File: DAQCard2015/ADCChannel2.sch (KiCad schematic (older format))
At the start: 16 parts, among them U17 THS4524IDBTR, U18 AD9219

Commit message: Various updates to DAQ board focusing on power system
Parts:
- U17: footprint Housings_SSOP:TSSOP-38_4.4x9.7mm_Pitch0.5mm -> extras:TSSOP-38_4.4x9.7mm_Pitch0.5mm
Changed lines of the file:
@@
 F 0 "U17" H 4700 2750 60  0000 C CNN
 F 1 "THS4524IDBTR" H 4400 4850 60  0000 C CNN
-F 2 "Housings_SSOP:TSSOP-38_4.4x9.7mm_Pitch0.5mm" H 4600 3800 60  0001 C CNN
+F 2 "extras:TSSOP-38_4.4x9.7mm_Pitch0.5mm" H 4600 3800 60  0001 C CNN
 F 3 "" H 4600 3800 60  0000 C CNN
 	1    4400 3700

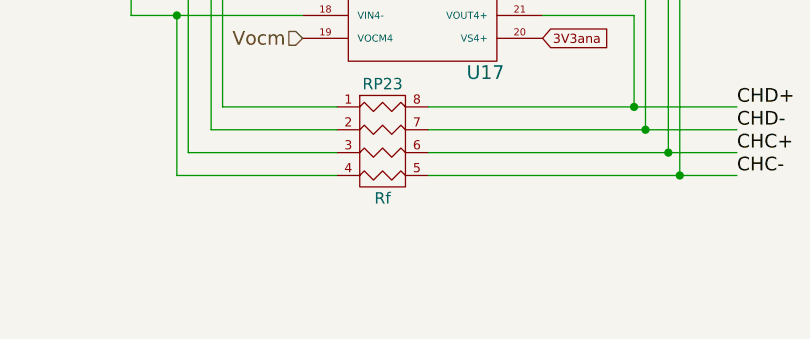
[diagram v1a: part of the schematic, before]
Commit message: Update to DAQ Board including adding an JTAG header and hooking up external clock and trigger
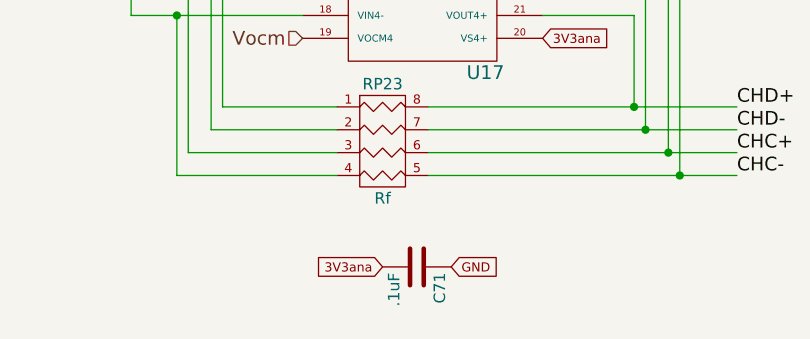
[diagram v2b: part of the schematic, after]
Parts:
- added C71: .1uF, Capacitors_SMD:C_0603, symbol C
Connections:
- net 3V3ana: now also C71.2
- net GND: now also C71.1
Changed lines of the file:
@@
 $Descr A4 11693 8268
 encoding utf-8
-Sheet 9 13
+Sheet 12 13
 Title ""
 Date ""
@@
 Text GLabel 8100 4150 0    40   Input ~ 0
 GND
+$Comp
+L C C71
+U 1 1 56064449
+P 4400 5500
+F 0 "C71" H 4425 5600 50  0000 L CNN
+F 1 ".1uF" H 4425 5400 50  0000 L CNN
+F 2 "Capacitors_SMD:C_0603" H 4438 5350 30  0001 C CNN
+F 3 "" H 4400 5500 60  0000 C CNN
+	1    4400 5500
+	0    1    1    0
+$EndComp
+Text GLabel 4250 5500 0    40   Input ~ 0
+3V3ana
+Text GLabel 4550 5500 2    40   Input ~ 0
+GND
 $EndSCHEMATC

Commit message: Adds digipart field to all parts that is now used in automatic generation of BOM(see DAQCard2015.html)
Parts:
- C47, C48, C49, C51, C52, C71: digipart (none) -> 445-1316-1-ND
- C50: digipart (none) -> 445-1420-1-ND
- R41, R42, R43, R44: digipart (none) -> P107HCT-ND
- R45: digipart (none) -> P10.0KHCT-ND
- RP22: digipart (none) -> RHM1564CT-ND
- RP23, RP24: digipart (none) -> RHM1336CT-ND
- U17: digipart (none) -> 296-24315-1-ND
- U18: digipart (none) -> AD9219ABCPZ-40-ND
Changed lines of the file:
@@
 F 2 "extras:QFN-48-1EP" H 8650 3700 60  0001 C CNN
 F 3 "" H 8650 3700 60  0000 C CNN
+F 4 "AD9219ABCPZ-40-ND" H 9050 3700 60  0001 C CNN "digipart"
 	1    9050 3700
 	1    0    0    -1
@@
 F 2 "Capacitors_SMD:C_0603" H 7588 3500 30  0001 C CNN
 F 3 "" H 7550 3650 60  0000 C CNN
+F 4 "445-1316-1-ND" H 7550 3650 60  0001 C CNN "digipart"
 	1    7550 3650
 	0    1    1    0
@@
 F 2 "Capacitors_SMD:C_0603" H 7588 3800 30  0001 C CNN
 F 3 "" H 7550 3950 60  0000 C CNN
+F 4 "445-1316-1-ND" H 7550 3950 60  0001 C CNN "digipart"
 	1    7550 3950
 	0    1    1    0
@@
 F 2 "Capacitors_SMD:C_0603" H 9338 1600 30  0001 C CNN
 F 3 "" H 9300 1750 60  0000 C CNN
+F 4 "445-1316-1-ND" H 9300 1750 60  0001 C CNN "digipart"
 	1    9300 1750
 	0    1    1    0
@@
 F 2 "Capacitors_SMD:C_0603" H 8638 1600 30  0001 C CNN
 F 3 "" H 8600 1750 60  0000 C CNN
+F 4 "445-1316-1-ND" H 8600 1750 60  0001 C CNN "digipart"
 	1    8600 1750
 	0    1    1    0
@@
 F 2 "Capacitors_SMD:C_0603" H 8988 1500 30  0001 C CNN
 F 3 "" H 8950 1650 60  0000 C CNN
+F 4 "445-1316-1-ND" H 8950 1650 60  0001 C CNN "digipart"
 	1    8950 1650
 	0    1    1    0
@@
 F 2 "Resistors_SMD:R_0603" V 9830 1950 30  0001 C CNN
 F 3 "" H 9900 1950 30  0000 C CNN
+F 4 "P10.0KHCT-ND" V 9900 1950 60  0001 C CNN "digipart"
 	1    9900 1950
 	0    1    1    0
@@
 F 2 "extras:TSSOP-38_4.4x9.7mm_Pitch0.5mm" H 4600 3800 60  0001 C CNN
 F 3 "" H 4600 3800 60  0000 C CNN
+F 4 "296-24315-1-ND" H 4400 3700 60  0001 C CNN "digipart"
 	1    4400 3700
 	1    0    0    -1
@@
 F 2 "Resistors_SMD:R_0603" V 1780 4350 30  0001 C CNN
 F 3 "" H 1850 4350 30  0000 C CNN
+F 4 "P107HCT-ND" V 1850 4350 60  0001 C CNN "digipart"
 	1    1850 4350
 	1    0    0    -1
@@
 F 2 "Resistors_SMD:R_0603" V 1780 3850 30  0001 C CNN
 F 3 "" H 1850 3850 30  0000 C CNN
+F 4 "P107HCT-ND" V 1850 3850 60  0001 C CNN "digipart"
 	1    1850 3850
 	1    0    0    -1
@@
 F 2 "Resistors_SMD:R_0603" V 1780 3350 30  0001 C CNN
 F 3 "" H 1850 3350 30  0000 C CNN
+F 4 "P107HCT-ND" V 1850 3350 60  0001 C CNN "digipart"
 	1    1850 3350
 	1    0    0    -1
@@
 F 2 "Resistors_SMD:R_0603" V 1780 2850 30  0001 C CNN
 F 3 "" H 1850 2850 30  0000 C CNN
+F 4 "P107HCT-ND" V 1850 2850 60  0001 C CNN "digipart"
 	1    1850 2850
 	1    0    0    -1
@@
 F 2 "extras:R4-MNR04" H 4250 5150 60  0001 C CNN
 F 3 "" H 4250 5150 60  0000 C CNN
+F 4 "RHM1336CT-ND" H 4250 5150 60  0001 C CNN "digipart"
 	1    4250 5150
 	1    0    0    -1
@@
 F 2 "extras:R4-MNR04" H 4300 2450 60  0001 C CNN
 F 3 "" H 4300 2450 60  0000 C CNN
+F 4 "RHM1336CT-ND" H 4300 2450 60  0001 C CNN "digipart"
 	1    4300 2450
 	1    0    0    -1
@@
 F 2 "extras:R8_MNR18" H 2750 3600 60  0001 C CNN
 F 3 "" H 2750 3600 60  0000 C CNN
+F 4 "RHM1564CT-ND" H 2750 3600 60  0001 C CNN "digipart"
 	1    2750 3600
 	1    0    0    -1
@@
 F 2 "Capacitors_SMD:C_0805" H 8988 1300 30  0001 C CNN
 F 3 "" H 8950 1450 60  0000 C CNN
+F 4 "445-1420-1-ND" H 8950 1450 60  0001 C CNN "digipart"
 	1    8950 1450
 	0    -1   -1   0
@@
 F 2 "Capacitors_SMD:C_0603" H 4438 5350 30  0001 C CNN
 F 3 "" H 4400 5500 60  0000 C CNN
+F 4 "445-1316-1-ND" H 4400 5500 60  0001 C CNN "digipart"
 	1    4400 5500
 	0    1    1    0

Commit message: annotates parts for new build-management tool
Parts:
- C47, C48, C49, C51, C52, C71: Digikey (none) -> 445-1316-1-ND; digipart 445-1316-1-ND -> (none)
- C50: Digikey (none) -> 445-1420-1-ND; digipart 445-1420-1-ND -> (none)
- R41, R42, R43, R44: Digikey (none) -> P107HCT-ND; digipart P107HCT-ND -> (none)
- R45: Digikey (none) -> P10.0KHCT-ND; digipart P10.0KHCT-ND -> (none)
- RP22: Digikey (none) -> RHM1564CT-ND; digipart RHM1564CT-ND -> (none)
- RP23, RP24: Digikey (none) -> RHM1336CT-ND; digipart RHM1336CT-ND -> (none)
- U17: Digikey (none) -> 296-24315-1-ND; digipart 296-24315-1-ND -> (none)
- U18: Digikey (none) -> AD9219ABCPZ-40-ND; digipart AD9219ABCPZ-40-ND -> (none)
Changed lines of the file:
@@
 EESchema Schematic File Version 2
+LIBS:DAQCard2015-rescue
 LIBS:power
 LIBS:device
@@
 F 2 "extras:QFN-48-1EP" H 8650 3700 60  0001 C CNN
 F 3 "" H 8650 3700 60  0000 C CNN
-F 4 "AD9219ABCPZ-40-ND" H 9050 3700 60  0001 C CNN "digipart"
+F 4 "AD9219ABCPZ-40-ND" H 9050 3700 60  0001 C CNN "Digikey"
 	1    9050 3700
 	1    0    0    -1
@@
 F 2 "Capacitors_SMD:C_0603" H 7588 3500 30  0001 C CNN
 F 3 "" H 7550 3650 60  0000 C CNN
-F 4 "445-1316-1-ND" H 7550 3650 60  0001 C CNN "digipart"
+F 4 "445-1316-1-ND" H 7550 3650 60  0001 C CNN "Digikey"
 	1    7550 3650
 	0    1    1    0
@@
 F 2 "Capacitors_SMD:C_0603" H 7588 3800 30  0001 C CNN
 F 3 "" H 7550 3950 60  0000 C CNN
-F 4 "445-1316-1-ND" H 7550 3950 60  0001 C CNN "digipart"
+F 4 "445-1316-1-ND" H 7550 3950 60  0001 C CNN "Digikey"
 	1    7550 3950
 	0    1    1    0
@@
 F 2 "Capacitors_SMD:C_0603" H 9338 1600 30  0001 C CNN
 F 3 "" H 9300 1750 60  0000 C CNN
-F 4 "445-1316-1-ND" H 9300 1750 60  0001 C CNN "digipart"
+F 4 "445-1316-1-ND" H 9300 1750 60  0001 C CNN "Digikey"
 	1    9300 1750
 	0    1    1    0
@@
 F 2 "Capacitors_SMD:C_0603" H 8638 1600 30  0001 C CNN
 F 3 "" H 8600 1750 60  0000 C CNN
-F 4 "445-1316-1-ND" H 8600 1750 60  0001 C CNN "digipart"
+F 4 "445-1316-1-ND" H 8600 1750 60  0001 C CNN "Digikey"
 	1    8600 1750
 	0    1    1    0
@@
 F 2 "Capacitors_SMD:C_0603" H 8988 1500 30  0001 C CNN
 F 3 "" H 8950 1650 60  0000 C CNN
-F 4 "445-1316-1-ND" H 8950 1650 60  0001 C CNN "digipart"
+F 4 "445-1316-1-ND" H 8950 1650 60  0001 C CNN "Digikey"
 	1    8950 1650
 	0    1    1    0
@@
 F 2 "Resistors_SMD:R_0603" V 9830 1950 30  0001 C CNN
 F 3 "" H 9900 1950 30  0000 C CNN
-F 4 "P10.0KHCT-ND" V 9900 1950 60  0001 C CNN "digipart"
+F 4 "P10.0KHCT-ND" V 9900 1950 60  0001 C CNN "Digikey"
 	1    9900 1950
 	0    1    1    0
@@
 F 2 "extras:TSSOP-38_4.4x9.7mm_Pitch0.5mm" H 4600 3800 60  0001 C CNN
 F 3 "" H 4600 3800 60  0000 C CNN
-F 4 "296-24315-1-ND" H 4400 3700 60  0001 C CNN "digipart"
+F 4 "296-24315-1-ND" H 4400 3700 60  0001 C CNN "Digikey"
 	1    4400 3700
 	1    0    0    -1
@@
 F 2 "Resistors_SMD:R_0603" V 1780 4350 30  0001 C CNN
 F 3 "" H 1850 4350 30  0000 C CNN
-F 4 "P107HCT-ND" V 1850 4350 60  0001 C CNN "digipart"
+F 4 "P107HCT-ND" V 1850 4350 60  0001 C CNN "Digikey"
 	1    1850 4350
 	1    0    0    -1
@@
 F 2 "Resistors_SMD:R_0603" V 1780 3850 30  0001 C CNN
 F 3 "" H 1850 3850 30  0000 C CNN
-F 4 "P107HCT-ND" V 1850 3850 60  0001 C CNN "digipart"
+F 4 "P107HCT-ND" V 1850 3850 60  0001 C CNN "Digikey"
 	1    1850 3850
 	1    0    0    -1
@@
 F 2 "Resistors_SMD:R_0603" V 1780 3350 30  0001 C CNN
 F 3 "" H 1850 3350 30  0000 C CNN
-F 4 "P107HCT-ND" V 1850 3350 60  0001 C CNN "digipart"
+F 4 "P107HCT-ND" V 1850 3350 60  0001 C CNN "Digikey"
 	1    1850 3350
 	1    0    0    -1
@@
 F 2 "Resistors_SMD:R_0603" V 1780 2850 30  0001 C CNN
 F 3 "" H 1850 2850 30  0000 C CNN
-F 4 "P107HCT-ND" V 1850 2850 60  0001 C CNN "digipart"
+F 4 "P107HCT-ND" V 1850 2850 60  0001 C CNN "Digikey"
 	1    1850 2850
 	1    0    0    -1
@@
 F 2 "extras:R4-MNR04" H 4250 5150 60  0001 C CNN
 F 3 "" H 4250 5150 60  0000 C CNN
-F 4 "RHM1336CT-ND" H 4250 5150 60  0001 C CNN "digipart"
+F 4 "RHM1336CT-ND" H 4250 5150 60  0001 C CNN "Digikey"
 	1    4250 5150
 	1    0    0    -1
@@
 F 2 "extras:R4-MNR04" H 4300 2450 60  0001 C CNN
 F 3 "" H 4300 2450 60  0000 C CNN
-F 4 "RHM1336CT-ND" H 4300 2450 60  0001 C CNN "digipart"
+F 4 "RHM1336CT-ND" H 4300 2450 60  0001 C CNN "Digikey"
 	1    4300 2450
 	1    0    0    -1
@@
 F 2 "extras:R8_MNR18" H 2750 3600 60  0001 C CNN
 F 3 "" H 2750 3600 60  0000 C CNN
-F 4 "RHM1564CT-ND" H 2750 3600 60  0001 C CNN "digipart"
+F 4 "RHM1564CT-ND" H 2750 3600 60  0001 C CNN "Digikey"
 	1    2750 3600
 	1    0    0    -1
@@
 F 2 "Capacitors_SMD:C_0805" H 8988 1300 30  0001 C CNN
 F 3 "" H 8950 1450 60  0000 C CNN
-F 4 "445-1420-1-ND" H 8950 1450 60  0001 C CNN "digipart"
+F 4 "445-1420-1-ND" H 8950 1450 60  0001 C CNN "Digikey"
 	1    8950 1450
 	0    -1   -1   0
@@
 F 2 "Capacitors_SMD:C_0603" H 4438 5350 30  0001 C CNN
 F 3 "" H 4400 5500 60  0000 C CNN
-F 4 "445-1316-1-ND" H 4400 5500 60  0001 C CNN "digipart"
+F 4 "445-1316-1-ND" H 4400 5500 60  0001 C CNN "Digikey"
 	1    4400 5500
 	0    1    1    0
